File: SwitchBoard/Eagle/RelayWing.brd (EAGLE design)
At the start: 51.7 x 55.9 mm, 29 parts, among them K1 EE2-3TNUH, K2 EE2-3TNUH, K3 EE2-3TNUH, K4 EE2-3TNUH, K5 EE2-3TNUH, U1 ULN2003ANS, U2 ULN2003ANS, U3 MCP23017SS, U4 INA219AID

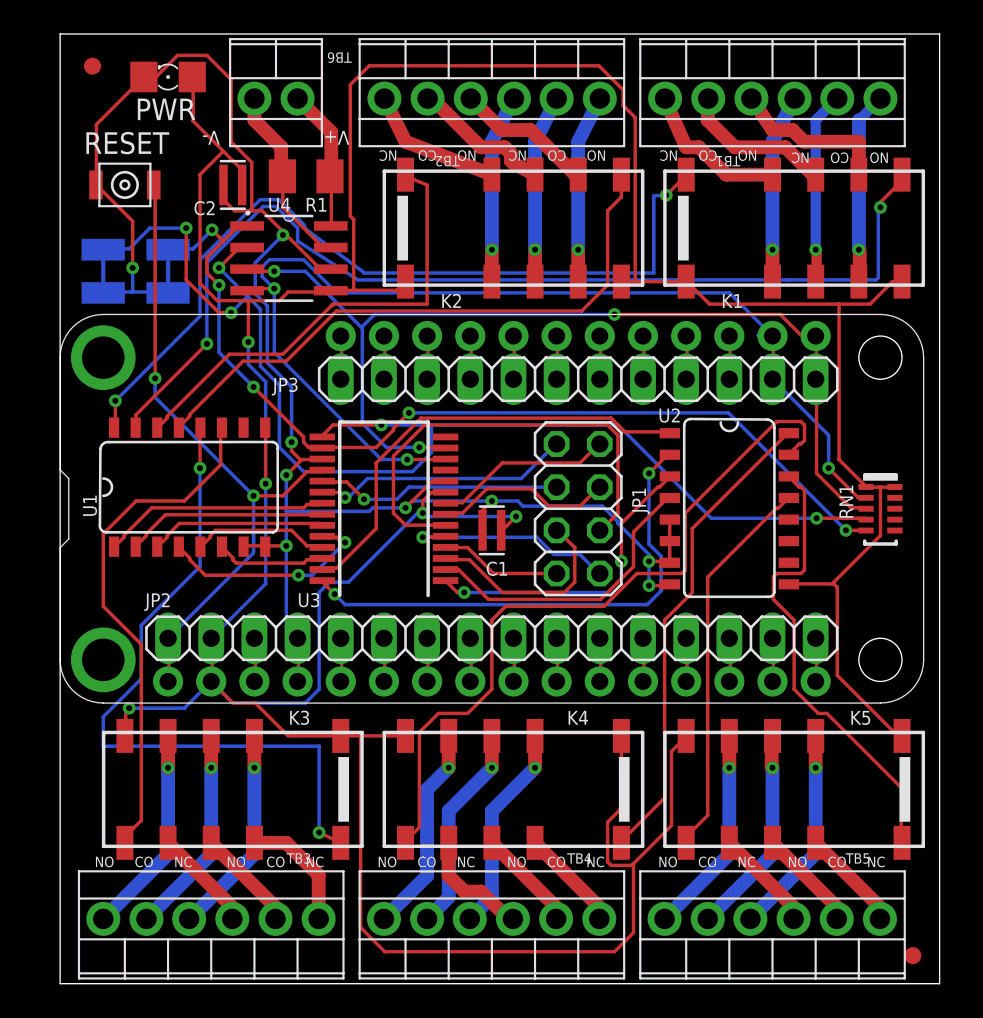
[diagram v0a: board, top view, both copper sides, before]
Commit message: Radius, labels, ERC
Corners radiused.
Relay labels added (ex Rly4).
Fixed one EDC warning.
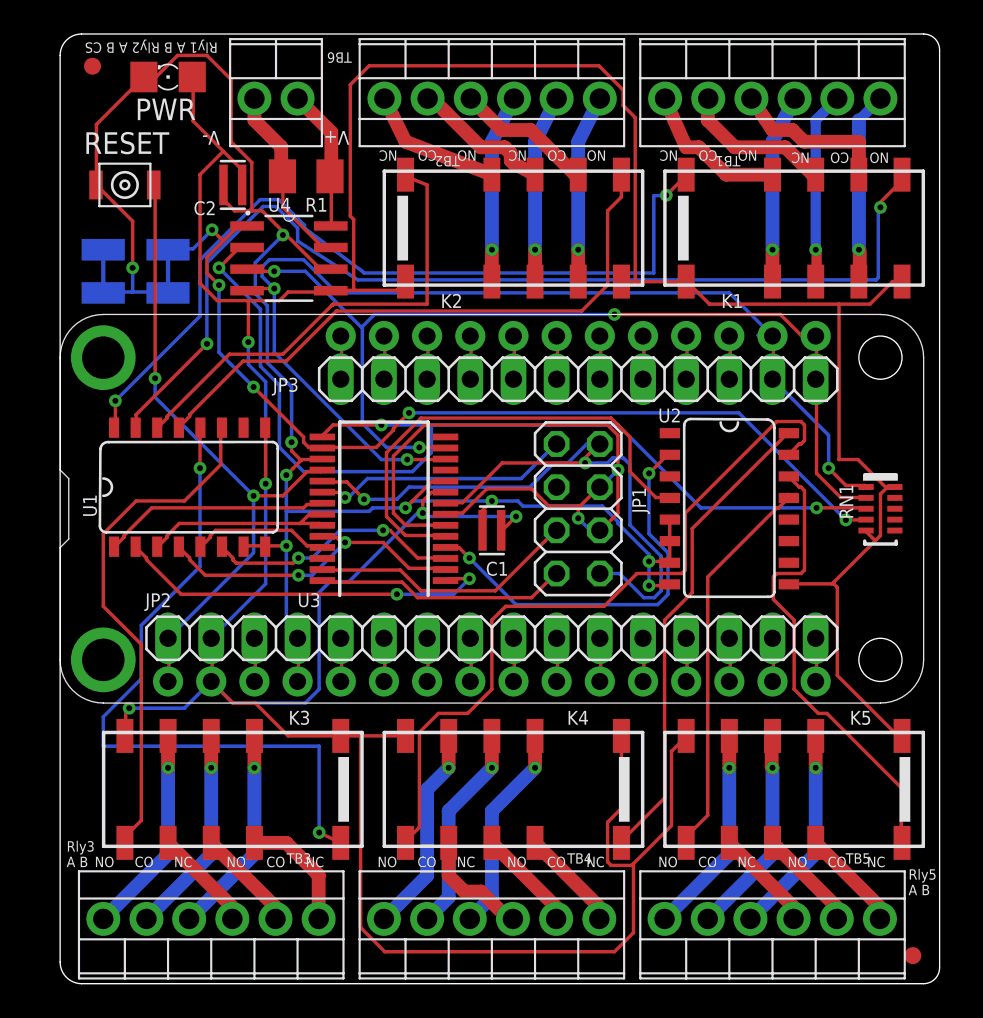
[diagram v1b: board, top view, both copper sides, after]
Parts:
- JP1: value (none) -> 2x4
- RN1: value CTS7461011 -> CTS746X101; device home:CTS746 -> home:CTS746X101
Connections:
- removed net GPB2: JP1.5, U3.3
- removed net GPB3: JP1.7, U3.4
- new net N$80: JP1.3, U3.26
- new net N$81: JP1.5, U3.27
- net 3V: now also RN1.5; no longer RN1.1
- net A0: now also RN1.3; no longer RN1.4
- net A1: now also RN1.4; no longer RN1.5
- net INTB: now also JP1.2; no longer JP1.3
- net N$63: now also U3.1; no longer U3.22
- net N$64: now also U3.22; no longer U3.23
- net N$65: now also U3.23; no longer U3.25
- net N$66: now also U3.3; no longer U3.26
- net N$67: now also U3.2; no longer U3.24
- net N$68: now also U3.24; no longer U3.27
- net N$69: now also U3.4; no longer U3.28
- net N$70: now also U3.25; no longer U3.1
- net N$71: now also U3.5; no longer U3.2
- net N$74: now also JP1.7, U3.28; no longer JP1.8, U3.5
- net N$75: now also JP1.4; no longer JP1.6
- net N$76: now also JP1.6; no longer JP1.4
- net N$77: now also JP1.8; no longer JP1.2
- net SCL: now also RN1.1; no longer RN1.2
- net SDA: now also RN1.2; no longer RN1.3
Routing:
- net N$68: track 26.8 -> 0.00 mm
- net N$70: track 18.2 -> 0.00 mm, vias 2 -> 0
- net N$81: track 0.00 -> 15.8 mm
- net N$77: track 10.5 -> 26.2 mm, vias 0 -> 1
- net A0: track 73.7 -> 60.2 mm, vias 5 -> 3
- net GPB2: track 12.2 -> 0.00 mm
- net N$63: track 11.8 -> 22.7 mm, vias 0 -> 2
- net N$71: track 17.6 -> 28.4 mm
- net N$66: track 6.49 -> 15.1 mm, vias 0 -> 2
- net GPB3: track 7.17 -> 0.00 mm
- net N$67: track 12.8 -> 19.4 mm
- net N$69: track 29.8 -> 24.0 mm
- net INTB: track 14.5 -> 18.1 mm
- net N$76: track 10.6 -> 12.8 mm, vias 0 -> 1
- net N$74: track 12.7 -> 14.8 mm, vias 1 -> 0
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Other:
- outline, holes or cut-outs redrawn
- board text added: "Rly1 A B Rly2 A B CS"
- board text added: "Rly3 A B"
- board text added: "Rly5 A B"

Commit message: No Air Wires
I worked out the air wires.  It's not pretty but it passes the DRC (except for the overlaps around the cut traces.
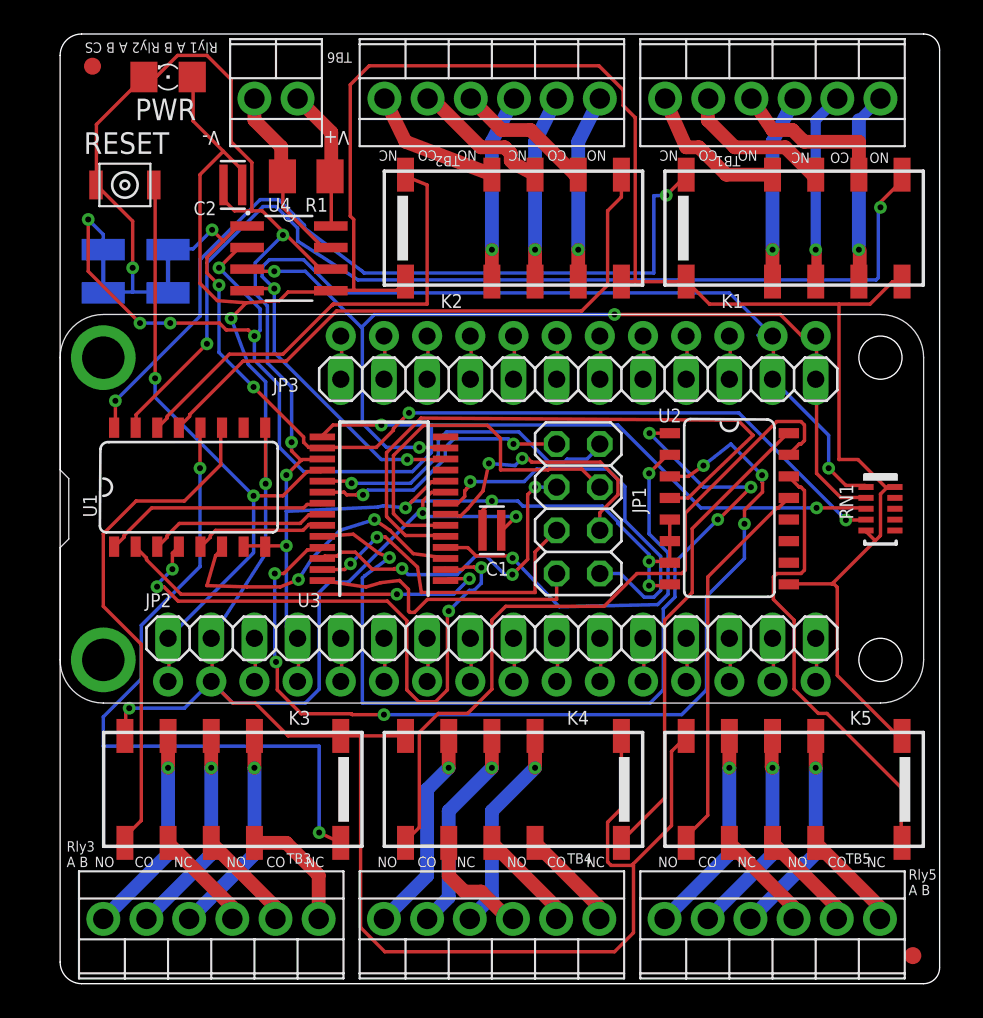
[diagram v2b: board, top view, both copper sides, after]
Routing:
- net N$70: track 0.00 -> 57.6 mm, vias 0 -> 6
- net N$68: track 0.00 -> 54.3 mm, vias 0 -> 4
- net N$80: track 0.00 -> 19.8 mm, vias 0 -> 3
- net A0: track 60.2 -> 77.2 mm, vias 3 -> 7
- net N$67: track 19.4 -> 36.3 mm, vias 2 -> 4
- net N$71: track 28.4 -> 36.9 mm
- net N$75: track 28.4 -> 22.3 mm, vias 1 -> 0
- net N$66: track 15.1 -> 18.9 mm
- net N$81: track 15.8 -> 19.5 mm, vias 0 -> 2
- net N$76: track 12.8 -> 16.3 mm, vias 1 -> 2
- net N$77: track 26.2 -> 23.6 mm
- net N$74: track 14.8 -> 17.3 mm
- net INTB: track 18.1 -> 19.4 mm
- net N$64: track 11.8 -> 10.5 mm
- net INTA: track 15.2 -> 15.9 mm, vias 1 -> 2

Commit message: Added 2x2 header & silkscreen changes
This is a version that has no airwires and has a 2x2 header with the I2C bus and power and ground pulled out.   It does NOT have John's part number changes that took place after 5/28
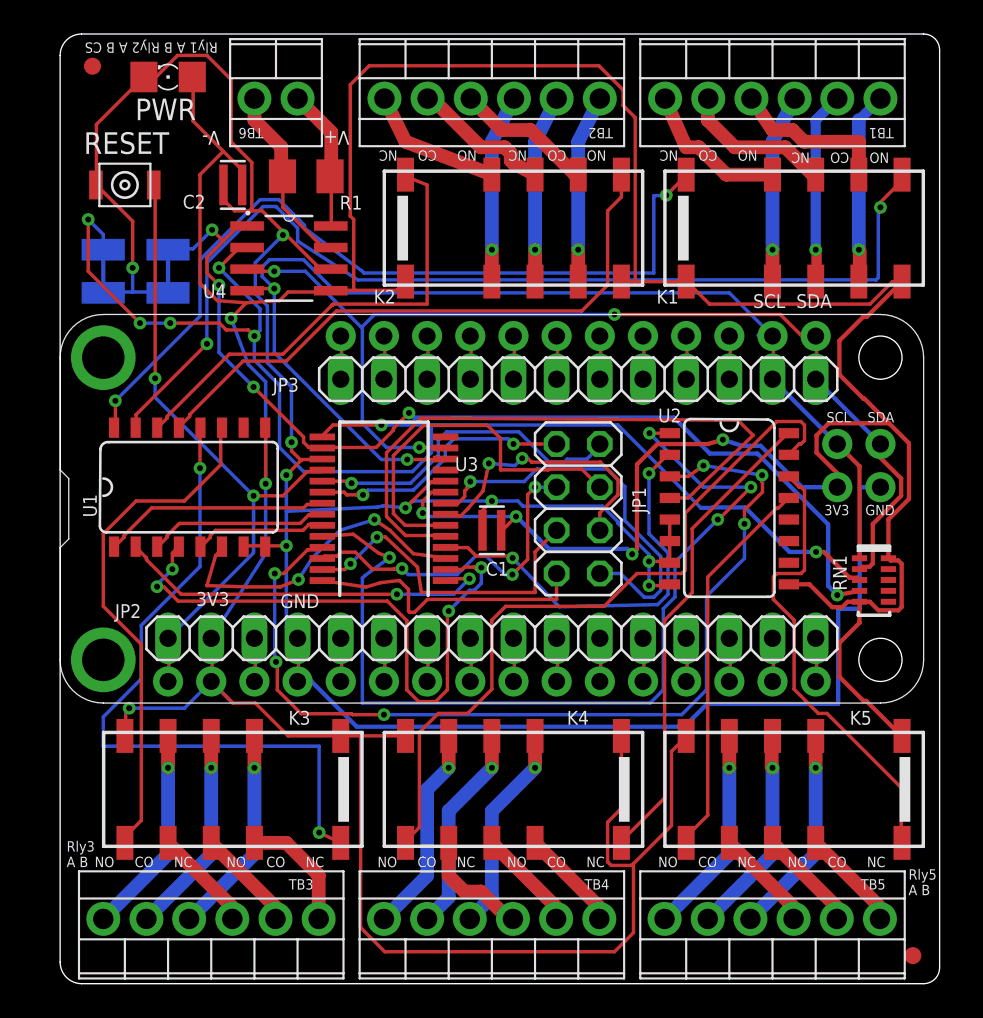
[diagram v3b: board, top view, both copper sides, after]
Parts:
- added JP4, JP5, JP6, JP7: (no value), adafruit:1X01-CLEANBIG
- moved RN1 4.21 mm to (47.9, 37.7)
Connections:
- net 3V: now also JP4.1
- net GND: now also JP5.1
- net SCL: now also JP6.1
- net SDA: now also JP7.1
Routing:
- net GND: track 109.6 -> 158.4 mm
- net 3V: track 249.8 -> 272.8 mm, vias 5 -> 7
- net SDA: track 58.5 -> 64.1 mm
- net A1: track 57.1 -> 60.7 mm
- net SCL: track 64.9 -> 68.2 mm, vias 3 -> 2
- net A0: track 77.2 -> 78.6 mm
- net N$70: track 57.6 -> 56.5 mm
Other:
- board text added: "3V3"
- board text added: "GND"
- board text added: "SCL"
- board text added: "SDA"
